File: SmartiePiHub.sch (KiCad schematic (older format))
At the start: 6 parts, among them P1 Conn_02x20_Odd_Even

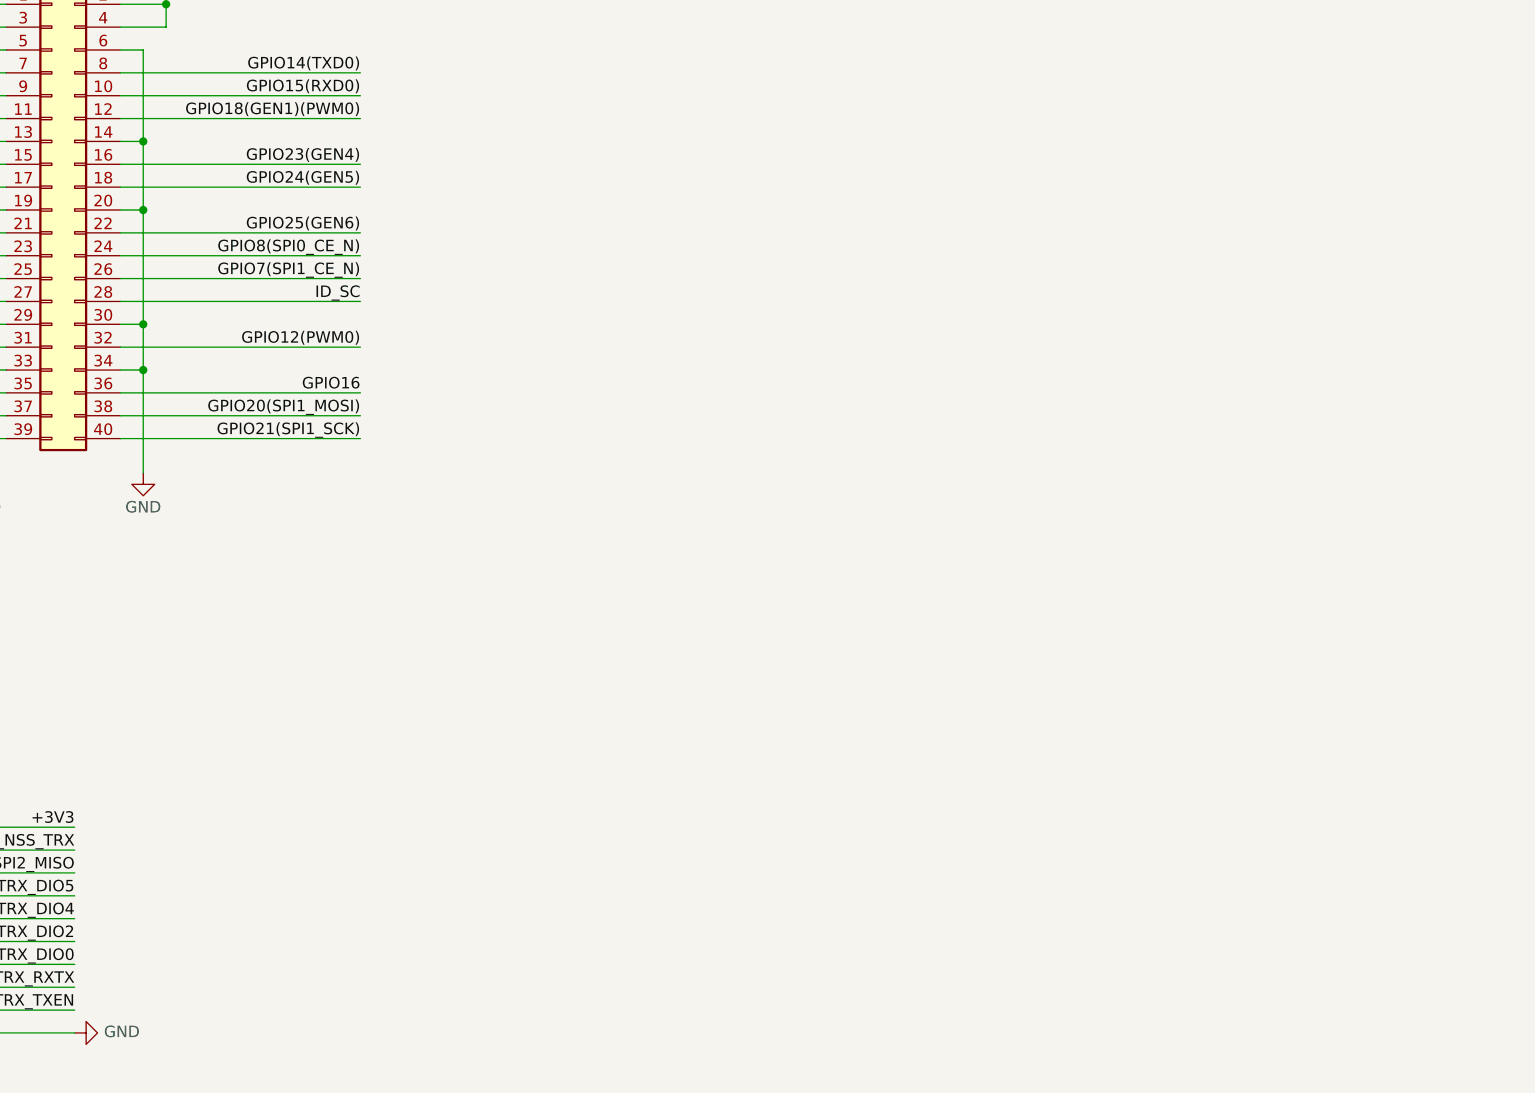
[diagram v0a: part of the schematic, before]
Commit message: added wm8960
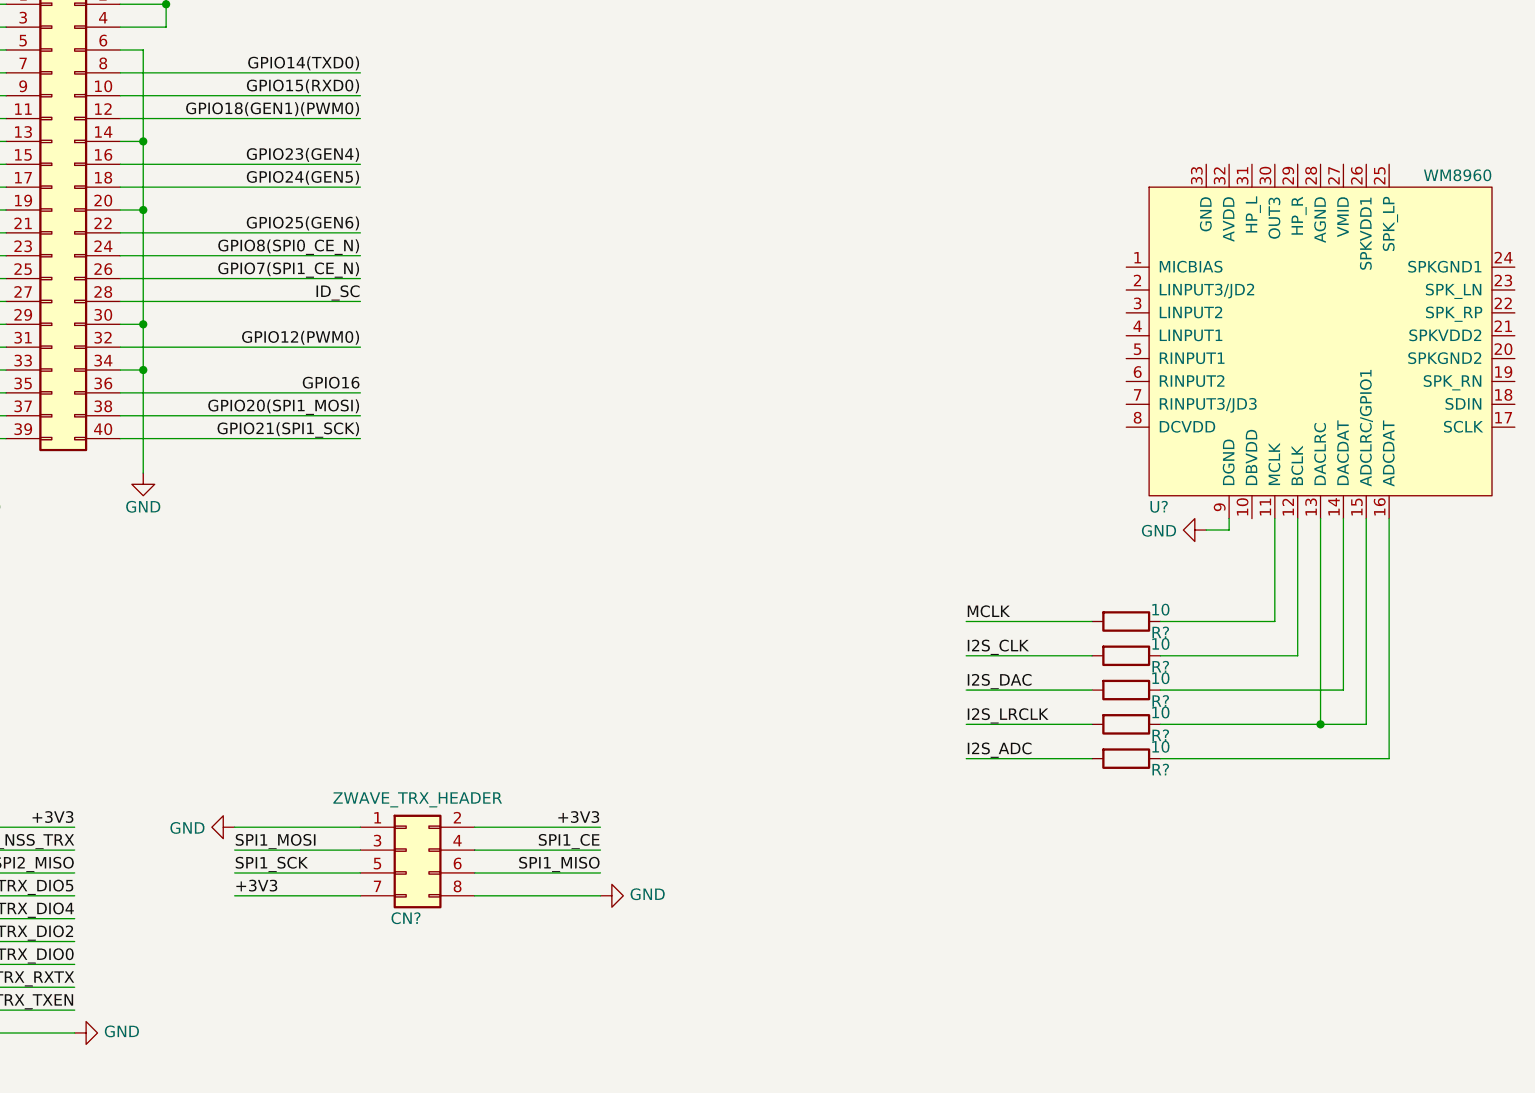
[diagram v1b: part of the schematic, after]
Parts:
- added CN?: ZWAVE_TRX_HEADER, symbol Connector_Generic:Conn_02x04_Odd_Even
- added R? (x5): 10, symbol Device:R
- added U?: WM8960, symbol smartie-pi-hub:WM8960
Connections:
- net +3V3: now also CN?.2 (Pin_2), CN?.7 (Pin_7)
- net GND: now also CN?.1 (Pin_1), CN?.8 (Pin_8), U?.9 (DGND)
- new net: R?.1, U?.11 (MCLK)
- new net: R?.1, U?.12 (BCLK)
- new net: R?.1, U?.13 (DACLRC), U?.15 (ADCLRC/GPIO1)
- new net: R?.1, U?.14 (DACDAT)
- new net: R?.1, U?.16 (ADCDAT)
- new net I2S_ADC: R?.2
- new net I2S_CLK: R?.2
- new net I2S_DAC: R?.2
- new net I2S_LRCLK: R?.2
- new net MCLK: R?.2
- new net SPI1_CE: CN?.4 (Pin_4)
- new net SPI1_MISO: CN?.6 (Pin_6)
- new net SPI1_MOSI: CN?.3 (Pin_3)
- new net SPI1_SCK: CN?.5 (Pin_5)
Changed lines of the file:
@@
 	0    1    1    0
 $EndComp
+$Comp
+L Connector_Generic:Conn_02x04_Odd_Even CN?
+U 1 1 5EB1A058
+P 4150 4800
+F 0 "CN?" H 4150 4500 50  0000 C CNN
+F 1 "ZWAVE_TRX_HEADER" H 4200 5026 50  0000 C CNN
+F 2 "" H 4150 4800 50  0001 C CNN
+F 3 "~" H 4150 4800 50  0001 C CNN
+	1    4150 4800
+	1    0    0    -1
+$EndComp
+Text Label 5000 4700 2    50   ~ 0
++3V3
+Wire Wire Line
+	5000 4700 4450 4700
+Text Label 5000 4800 2    50   ~ 0
+SPI1_CE
+Wire Wire Line
+	5000 4800 4450 4800
+Text Label 5000 4900 2    50   ~ 0
+SPI1_MISO
+Wire Wire Line
+	5000 4900 4450 4900
+Wire Wire Line
+	5000 5000 4450 5000
+$Comp
+L power:GND #PWR?
+U 1 1 5EB24C87
+P 5000 5000
+F 0 "#PWR?" H 5000 4750 50  0001 C CNN
+F 1 "GND" V 5005 4872 50  0000 R CNN
+F 2 "" H 5000 5000 50  0001 C CNN
+F 3 "" H 5000 5000 50  0001 C CNN
+	1    5000 5000
+	0    -1   -1   0
+$EndComp
+Wire Wire Line
+	3950 4700 3400 4700
+$Comp
+L power:GND #PWR?
+U 1 1 5EB277F2
+P 3400 4700
+F 0 "#PWR?" H 3400 4450 50  0001 C CNN
+F 1 "GND" V 3405 4572 50  0000 R CNN
+F 2 "" H 3400 4700 50  0001 C CNN
+F 3 "" H 3400 4700 50  0001 C CNN
+	1    3400 4700
+	0    1    1    0
+$EndComp
+Text Label 3400 4800 0    50   ~ 0
+SPI1_MOSI
+Wire Wire Line
+	3950 4800 3400 4800
+Wire Wire Line
+	3950 4900 3400 4900
+Text Label 3400 4900 0    50   ~ 0
+SPI1_SCK
+Text Label 3400 5000 0    50   ~ 0
++3V3
+Wire Wire Line
+	3950 5000 3400 5000
+$Comp
+L smartie-pi-hub:WM8960 U?
+U 1 1 5EB45B26
+P 8100 2200
+F 0 "U?" H 7400 1100 50  0000 L CNN
+F 1 "WM8960" H 8600 2550 50  0000 L CNN
+F 2 "" H 8100 2200 50  0001 C CNN
+F 3 "" H 8100 2200 50  0001 C CNN
+	1    8100 2200
+	1    0    0    -1
+$EndComp
+$Comp
+L Device:R R?
+U 1 1 5EB5603D
+P 7300 3800
+F 0 "R?" V 7350 3950 50  0000 C CNN
+F 1 "10" V 7250 3950 50  0000 C CNN
+F 2 "" V 7230 3800 50  0001 C CNN
+F 3 "~" H 7300 3800 50  0001 C CNN
+	1    7300 3800
+	0    1    1    0
+$EndComp
+$Comp
+L Device:R R?
+U 1 1 5EB5735D
+P 7300 3950
+F 0 "R?" V 7350 4100 50  0000 C CNN
+F 1 "10" V 7250 4100 50  0000 C CNN
+F 2 "" V 7230 3950 50  0001 C CNN
+F 3 "~" H 7300 3950 50  0001 C CNN
+	1    7300 3950
+	0    1    1    0
+$EndComp
+$Comp
+L Device:R R?
+U 1 1 5EB5A3A5
+P 7300 4100
+F 0 "R?" V 7350 4250 50  0000 C CNN
+F 1 "10" V 7250 4250 50  0000 C CNN
+F 2 "" V 7230 4100 50  0001 C CNN
+F 3 "~" H 7300 4100 50  0001 C CNN
+	1    7300 4100
+	0    1    1    0
+$EndComp
+$Comp
+L Device:R R?
+U 1 1 5EB5CCB9
+P 7300 4250
+F 0 "R?" V 7350 4400 50  0000 C CNN
+F 1 "10" V 7250 4400 50  0000 C CNN
+F 2 "" V 7230 4250 50  0001 C CNN
+F 3 "~" H 7300 4250 50  0001 C CNN
+	1    7300 4250
+	0    1    1    0
+$EndComp
+$Comp
+L Device:R R?
+U 1 1 5EB5F5F9
+P 7300 4400
+F 0 "R?" V 7350 4550 50  0000 C CNN
+F 1 "10" V 7250 4550 50  0000 C CNN
+F 2 "" V 7230 4400 50  0001 C CNN
+F 3 "~" H 7300 4400 50  0001 C CNN
+	1    7300 4400
+	0    1    1    0
+$EndComp
+Wire Wire Line
+	7950 3350 7950 3800
+Wire Wire Line
+	7950 3800 7450 3800
+Wire Wire Line
+	8450 3350 8450 4400
+Wire Wire Line
+	8450 4400 7450 4400
+Wire Wire Line
+	8350 3350 8350 4250
+Wire Wire Line
+	8350 4250 8150 4250
+Wire Wire Line
+	8150 3350 8150 4250
+Connection ~ 8150 4250
+Wire Wire Line
+	8150 4250 7450 4250
+Wire Wire Line
+	7450 4100 8250 4100
+Wire Wire Line
+	8250 4100 8250 3350
+Wire Wire Line
+	8050 3350 8050 3950
+Wire Wire Line
+	8050 3950 7450 3950
+Wire Wire Line
+	7750 3350 7750 3400
+Wire Wire Line
+	7750 3400 7650 3400
+$Comp
+L power:GND #PWR?
+U 1 1 5EBF331B
+P 7650 3400
+F 0 "#PWR?" H 7650 3150 50  0001 C CNN
+F 1 "GND" V 7655 3272 50  0000 R CNN
+F 2 "" H 7650 3400 50  0001 C CNN
+F 3 "" H 7650 3400 50  0001 C CNN
+	1    7650 3400
+	0    1    1    0
+$EndComp
+Wire Wire Line
+	7150 3800 6600 3800
+Text Label 6600 3800 0    50   ~ 0
+MCLK
+Wire Wire Line
+	7150 3950 6600 3950
+Text Label 6600 3950 0    50   ~ 0
+I2S_CLK
+Wire Wire Line
+	7150 4100 6600 4100
+Text Label 6600 4100 0    50   ~ 0
+I2S_DAC
+Wire Wire Line
+	7150 4250 6600 4250
+Text Label 6600 4250 0    50   ~ 0
+I2S_LRCLK
+Wire Wire Line
+	7150 4400 6600 4400
+Text Label 6600 4400 0    50   ~ 0
+I2S_ADC
 $EndSCHEMATC

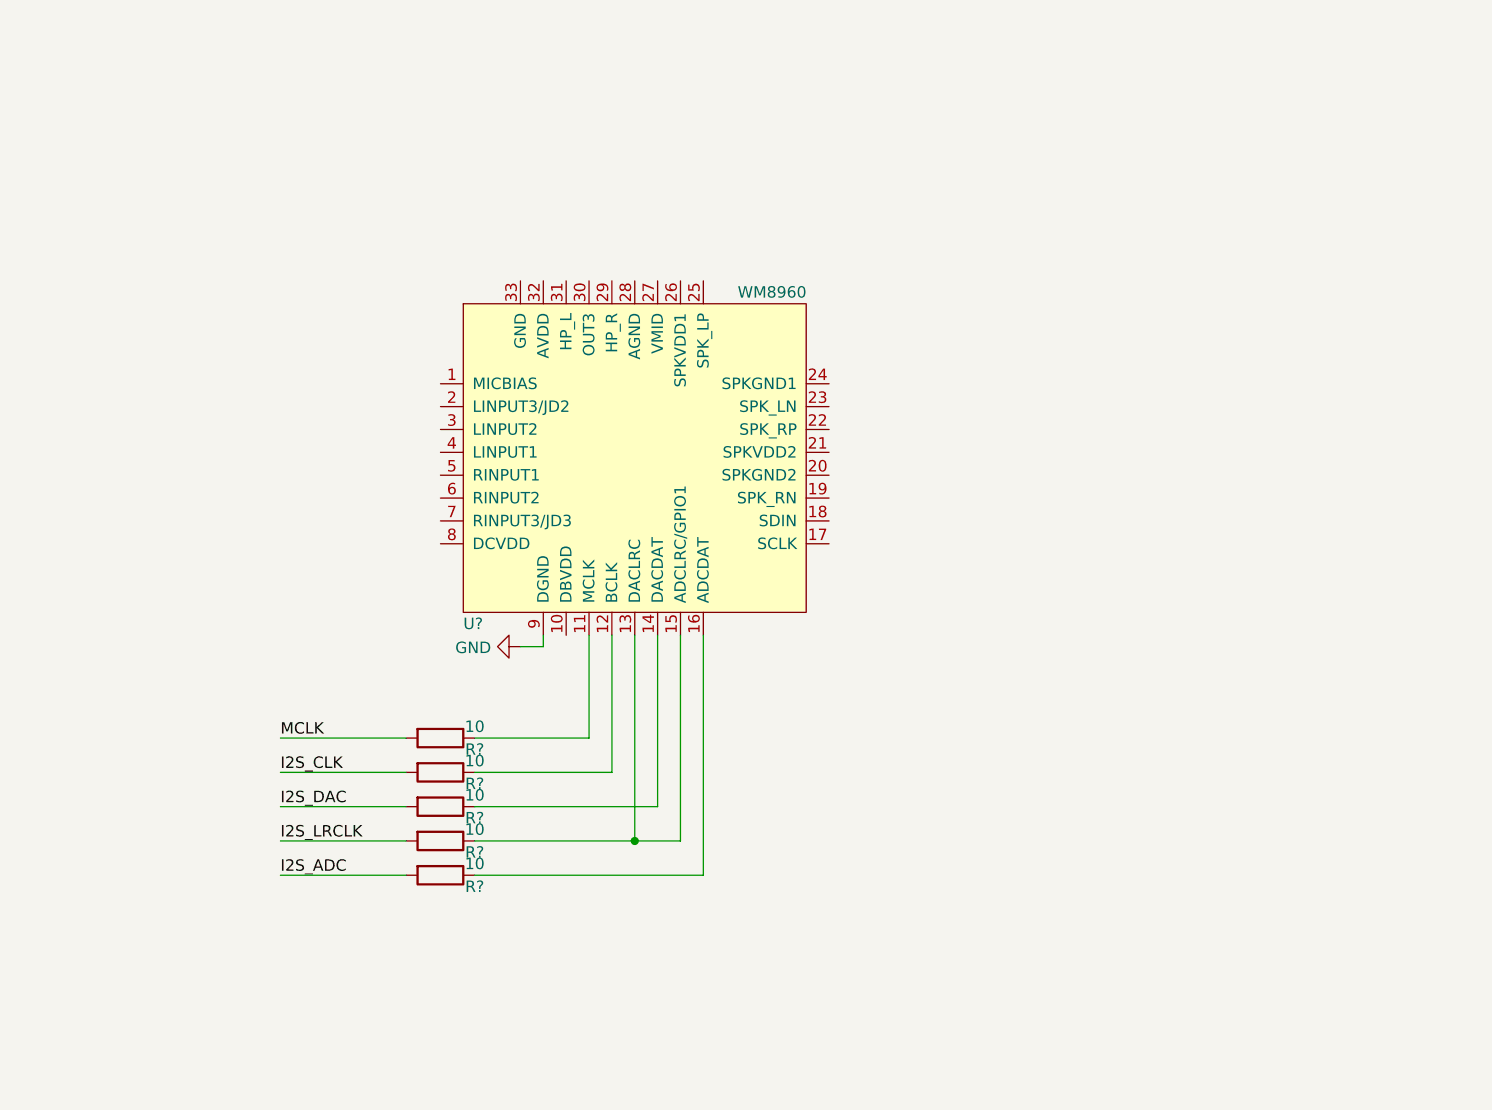
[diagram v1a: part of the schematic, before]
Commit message: more work on wm8960
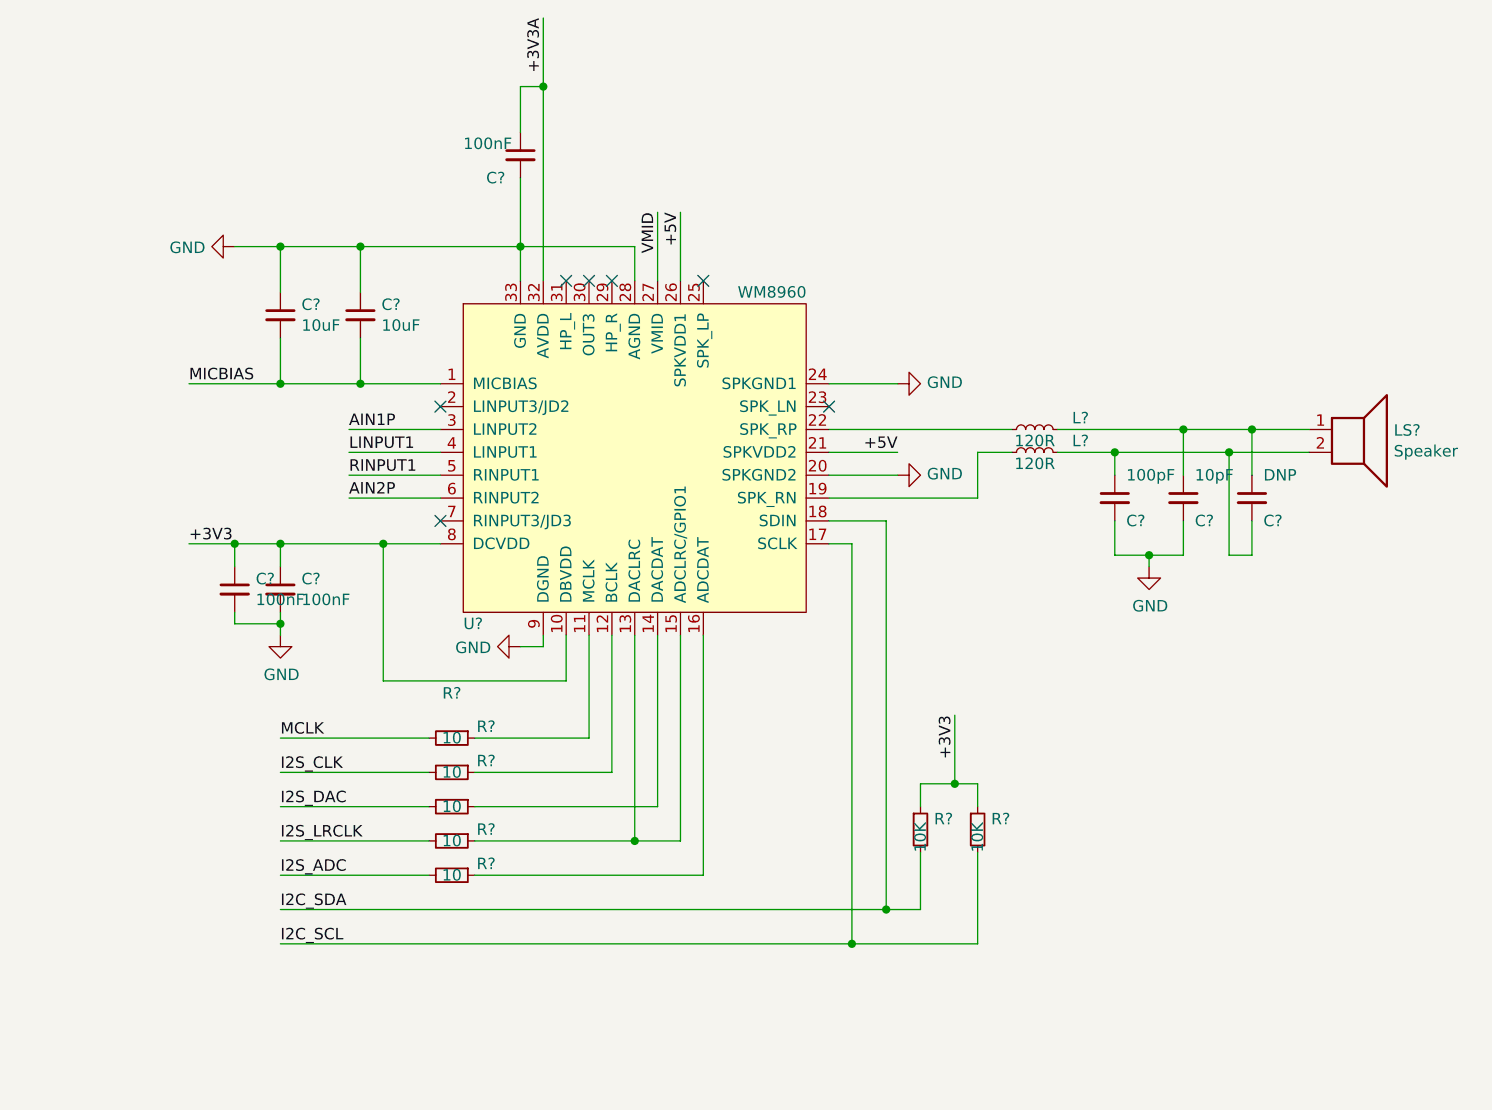
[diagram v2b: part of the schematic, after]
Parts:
- removed R? (x5): 10, symbol Device:R
- added C? (x3): 100nF, symbol Device:C_Small
- added C? (x2): 10uF, symbol Device:C_Small
- added C?: 100pF, symbol Device:C_Small
- added C?: 10pF, symbol Device:C_Small
- added C?: DNP, symbol Device:C_Small
- added L? (x2): 120R, symbol Device:L_Small
- added LS?: Speaker, symbol Device:Speaker
- added R? (x2): 10K, symbol Device:R_Small
- added R? (x5): 10, symbol Device:R_Small
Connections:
- net +3V3: now also U?.10 (DBVDD), U?.8 (DCVDD), C?.1, C?.1, R?.1, R?.1
- net +5V: now also U?.21 (SPKVDD2), U?.26 (SPKVDD1)
- net GND: now also U?.20 (SPKGND2), U?.24 (SPKGND1), U?.28 (AGND), U?.33 (GND), C?.1, C?.1, C?.2, C?.2, C?.2, C?.2, C?.2
- net I2S_ADC: now also R?.2
- net I2S_CLK: now also R?.2
- net I2S_DAC: now also R?.2
- net I2S_LRCLK: now also R?.2
- net MCLK: now also R?.2
- net MICBIAS: now reaches U?.1 (MICBIAS)
- net MICBIAS: now also C?.2, C?.2
- net at U?.11 (MCLK): now also R?.1
- net at U?.12 (BCLK): now also R?.1
- net at U?.13 (DACLRC), U?.15 (ADCLRC/GPIO1): now also R?.1
- net at U?.14 (DACDAT): now also R?.1
- net at U?.16 (ADCDAT): now also R?.1
- net I2C_SCL: now reaches U?.17 (SCLK)
- net I2C_SCL: now also R?.2
- net I2C_SDA: now reaches U?.18 (SDIN)
- net I2C_SDA: now also R?.2
- net at U?.19 (SPK_RN): now also L?.1
- net at U?.22 (SPK_RP): now also L?.1
- net VMID: now reaches U?.27 (VMID)
- net AIN1P: now reaches U?.3 (LINPUT2)
- net +3V3A: now reaches U?.32 (AVDD)
- net +3V3A: now also C?.1
- net LINPUT1: now reaches U?.4 (LINPUT1)
- net RINPUT1: now reaches U?.5 (RINPUT1)
- net AIN2P: now reaches U?.6 (RINPUT2)
- new net: C?.1, C?.1, L?.2, LS?.1
- new net: C?.1, C?.2, L?.2, LS?.2
- no-connect marks 0 -> 7
